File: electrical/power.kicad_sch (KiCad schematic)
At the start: 61 parts

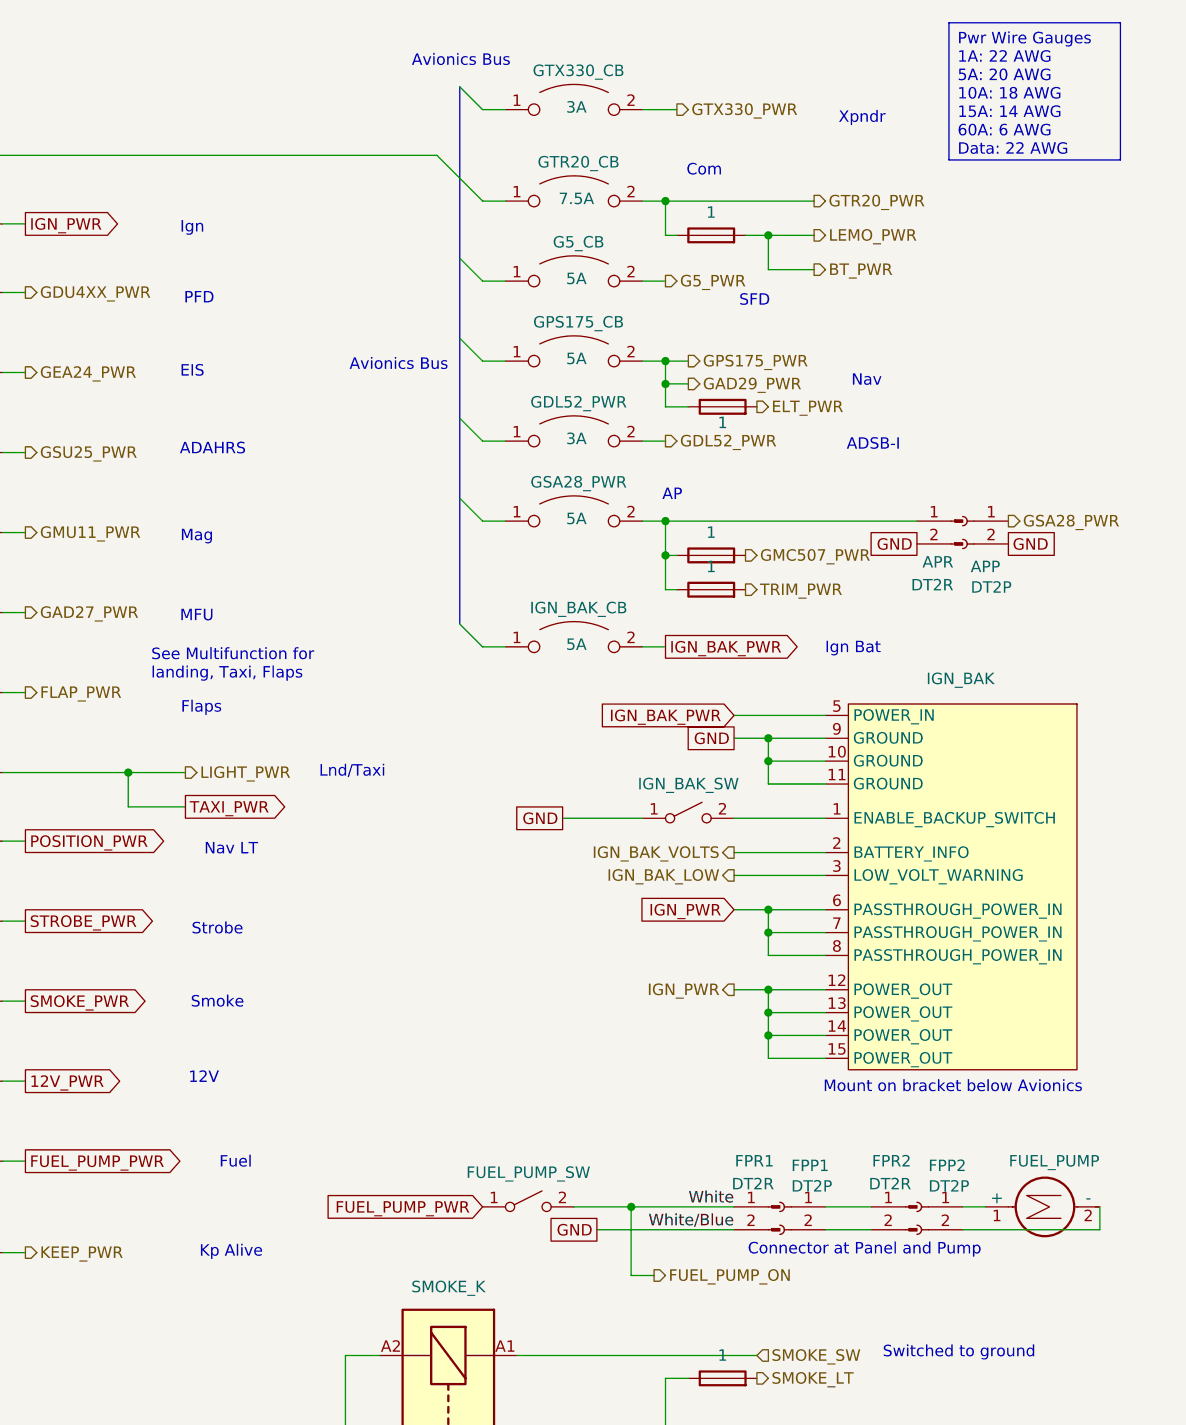
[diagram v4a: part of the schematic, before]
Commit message: Added AWG wires.
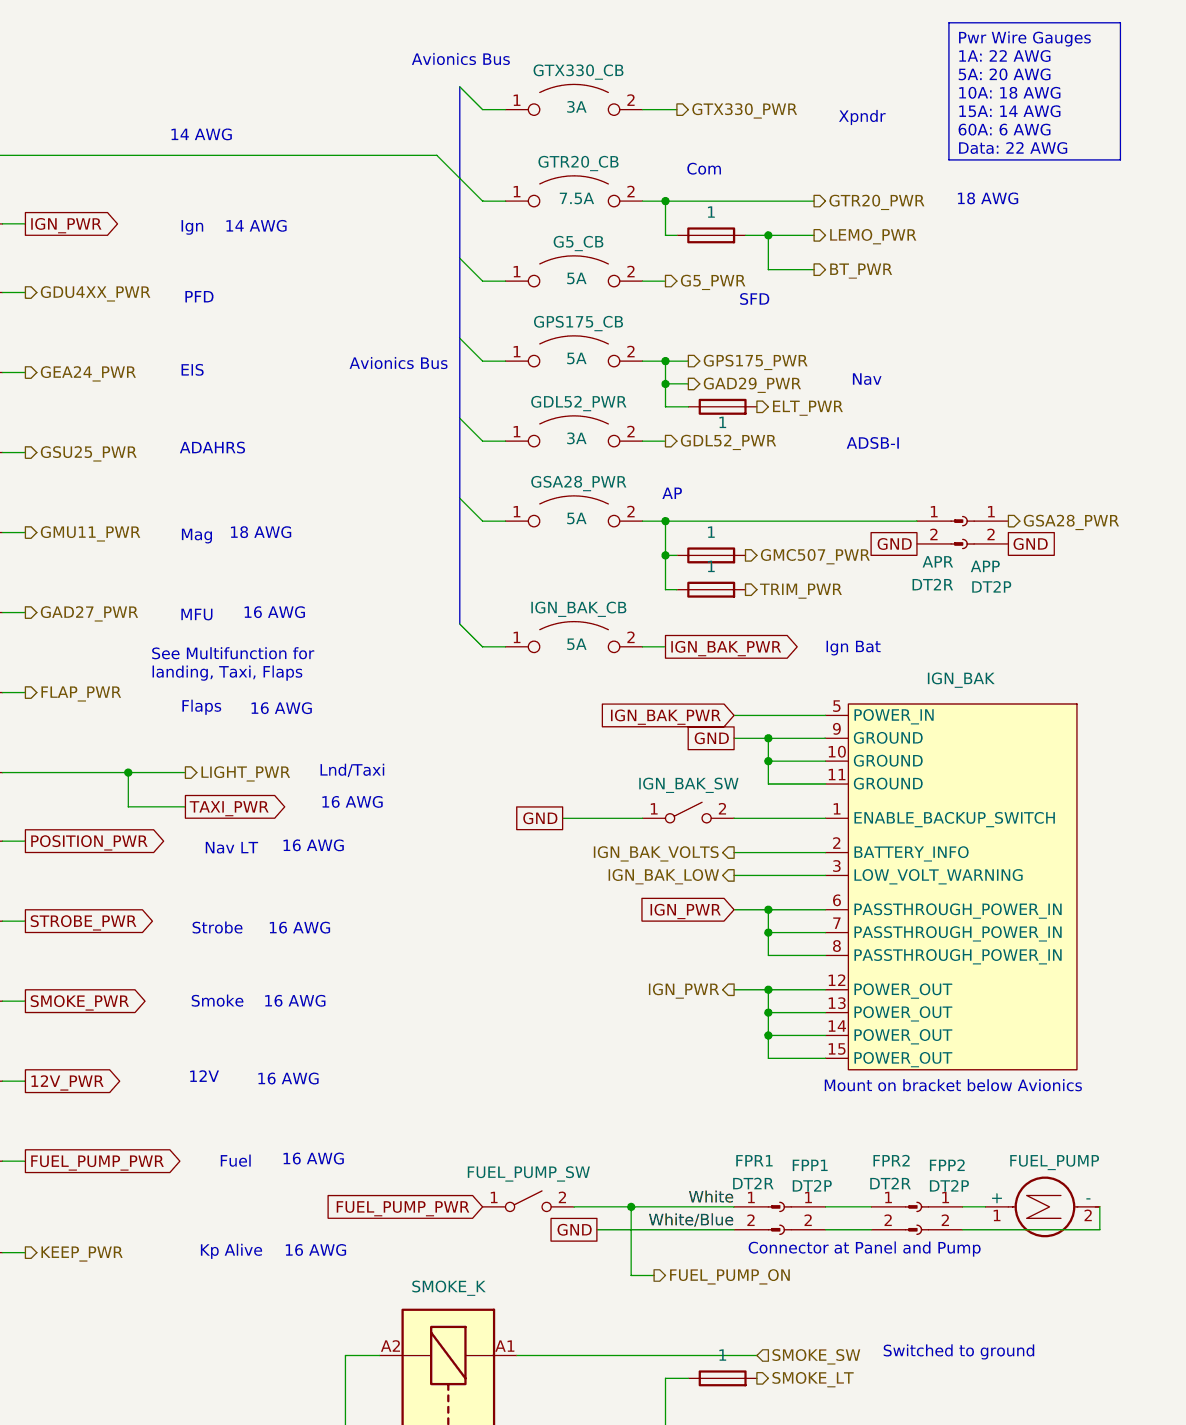
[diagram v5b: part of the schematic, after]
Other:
- note added: "14 AWG"
- note added: "16 AWG"
- note added: "18 AWG"
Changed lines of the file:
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@@
 		(title "Power Distribution")
 		(date "2025-12-24")
-		(rev "1.2")
+		(rev "1.2.1")
 		(company "N877RV")
 	)
@@
 		)
 	)
+	(text "16 AWG"
+		(exclude_from_sim no)
+		(at 109.982 123.444 0)
+		(effects
+			(font
+				(size 1.27 1.27)
+			)
+		)
+	)
 	(text "ADAHRS"
 		(exclude_from_sim no)
@@
 		)
 	)
+	(text "18 AWG"
+		(exclude_from_sim no)
+		(at 106.172 71.374 0)
+		(effects
+			(font
+				(size 1.27 1.27)
+			)
+		)
+	)
 	(text "Install small fuse box with 6 1A fuses\nInstall ground bar on both sides of firewall with 6AWG between"
 		(exclude_from_sim no)
@@
 		)
 	)
+	(text "16 AWG"
+		(exclude_from_sim no)
+		(at 107.696 80.264 0)
+		(effects
+			(font
+				(size 1.27 1.27)
+			)
+		)
+	)
 	(text "Nav"
 		(exclude_from_sim no)
@@
 		)
 	)
+	(text "16 AWG"
+		(exclude_from_sim no)
+		(at 109.22 132.08 0)
+		(effects
+			(font
+				(size 1.27 1.27)
+			)
+		)
+	)
 	(text "Ign"
 		(exclude_from_sim no)
@@
 		)
 	)
+	(text "14 AWG"
+		(exclude_from_sim no)
+		(at 99.568 27.178 0)
+		(effects
+			(font
+				(size 1.27 1.27)
+			)
+		)
+	)
+	(text "16 AWG"
+		(exclude_from_sim no)
+		(at 108.458 90.932 0)
+		(effects
+			(font
+				(size 1.27 1.27)
+			)
+		)
+	)
+	(text "16 AWG"
+		(exclude_from_sim no)
+		(at 112.014 140.97 0)
+		(effects
+			(font
+				(size 1.27 1.27)
+			)
+		)
+	)
+	(text "16 AWG"
+		(exclude_from_sim no)
+		(at 112.014 106.172 0)
+		(effects
+			(font
+				(size 1.27 1.27)
+			)
+		)
+	)
 	(text "Connector at Panel and Pump"
 		(exclude_from_sim no)
@@
 		)
 	)
+	(text "16 AWG"
+		(exclude_from_sim no)
+		(at 112.268 151.13 0)
+		(effects
+			(font
+				(size 1.27 1.27)
+			)
+		)
+	)
 	(text "Strobe"
 		(exclude_from_sim no)
@@
 		)
 	)
+	(text "16 AWG"
+		(exclude_from_sim no)
+		(at 116.332 101.346 0)
+		(effects
+			(font
+				(size 1.27 1.27)
+			)
+		)
+	)
 	(text "Switched to ground"
 		(exclude_from_sim no)
@@
 		)
 	)
+	(text "18 AWG"
+		(exclude_from_sim no)
+		(at 186.944 34.29 0)
+		(effects
+			(font
+				(size 1.27 1.27)
+			)
+		)
+	)
 	(text "Connector at Panel"
 		(exclude_from_sim no)
@@
 		)
 	)
+	(text "14 AWG"
+		(exclude_from_sim no)
+		(at 105.664 37.338 0)
+		(effects
+			(font
+				(size 1.27 1.27)
+			)
+		)
+	)
 	(text "Fuel"
 		(exclude_from_sim no)
@@
 		(effects
 			(font
+				(size 1.27 1.27)
+			)
+		)
+	)
+	(text "16 AWG"
+		(exclude_from_sim no)
+		(at 110.49 115.316 0)
+		(effects
+			(font

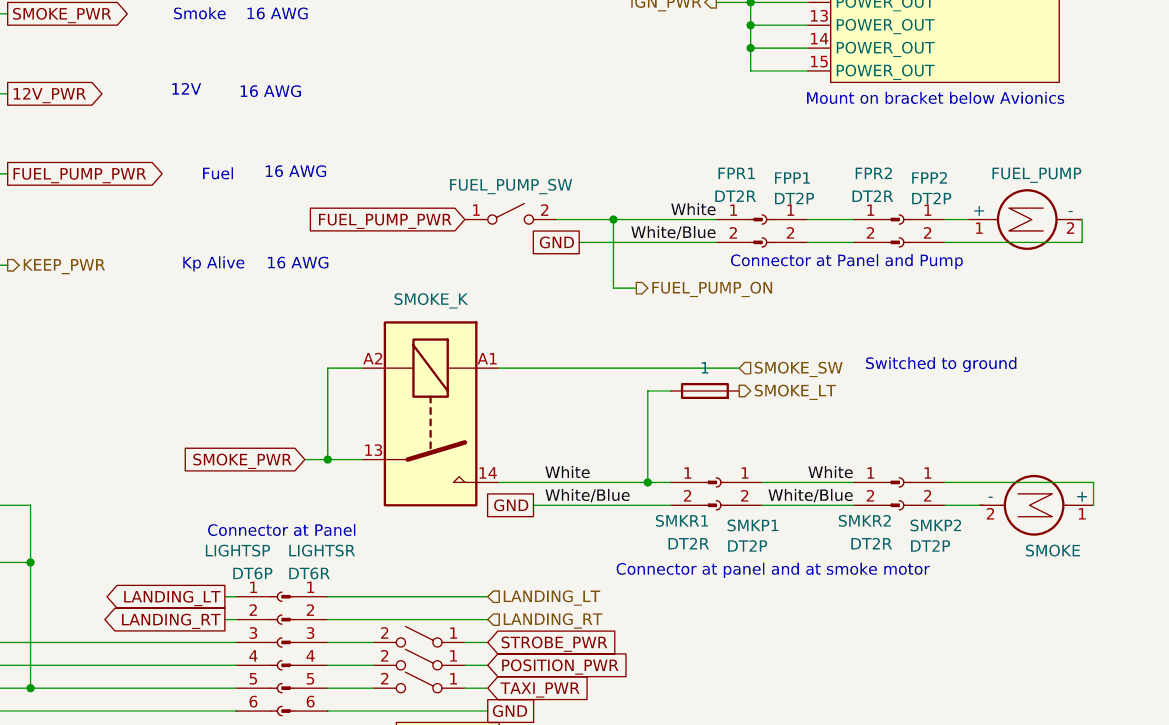
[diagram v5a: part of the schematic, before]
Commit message: Added extra connector for GDL 52, rewired stick to have flaps up/down instead of level/smoke. Put smoke on panel.
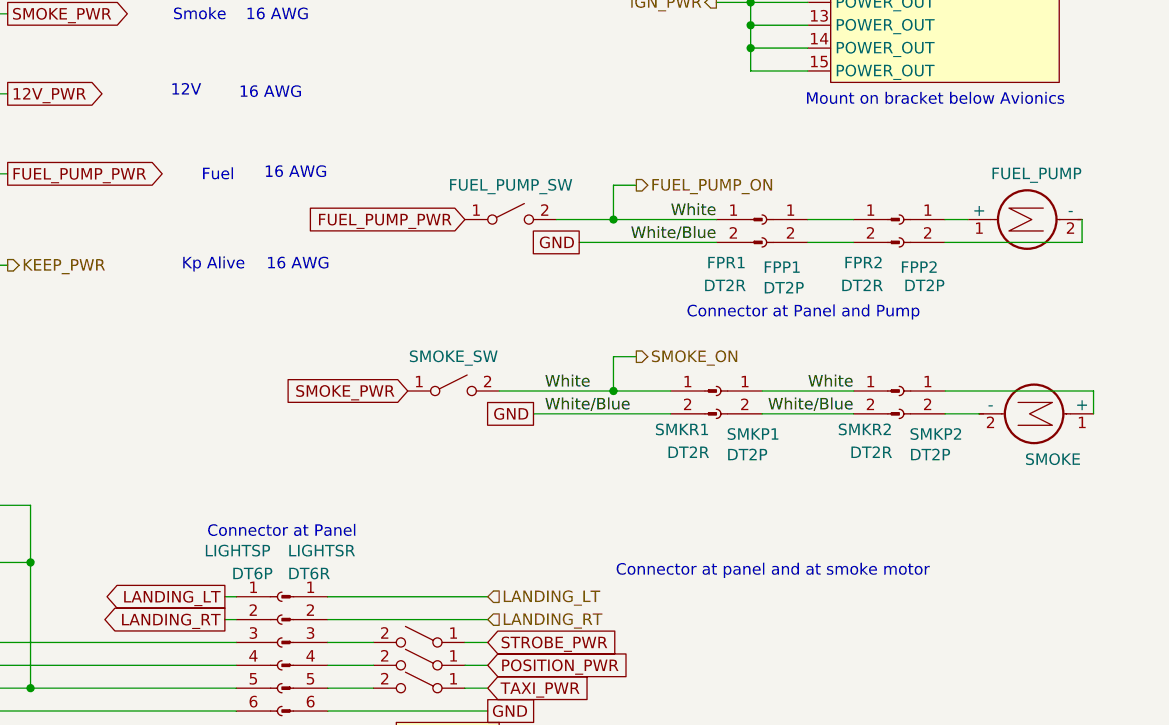
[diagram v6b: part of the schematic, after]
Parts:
- removed SMOKE_K: Relay_SPST-NO, symbol Relay:Relay_SPST-NO
- removed SMOKE_LT_FS: 1, symbol Device:Fuse
- added SMOKE_SW: ~, symbol Switch:SW_SPST
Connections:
- net FUEL_PUMP_ON: now also SMOKE_SW.2 (B)
- net SMOKE_PWR: now also SMOKE_SW.1 (A)
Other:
- note removed: "Switched to ground"
- moved on the sheet: SMKP1, SMKP2, SMKR1, SMKR2, SMOKE

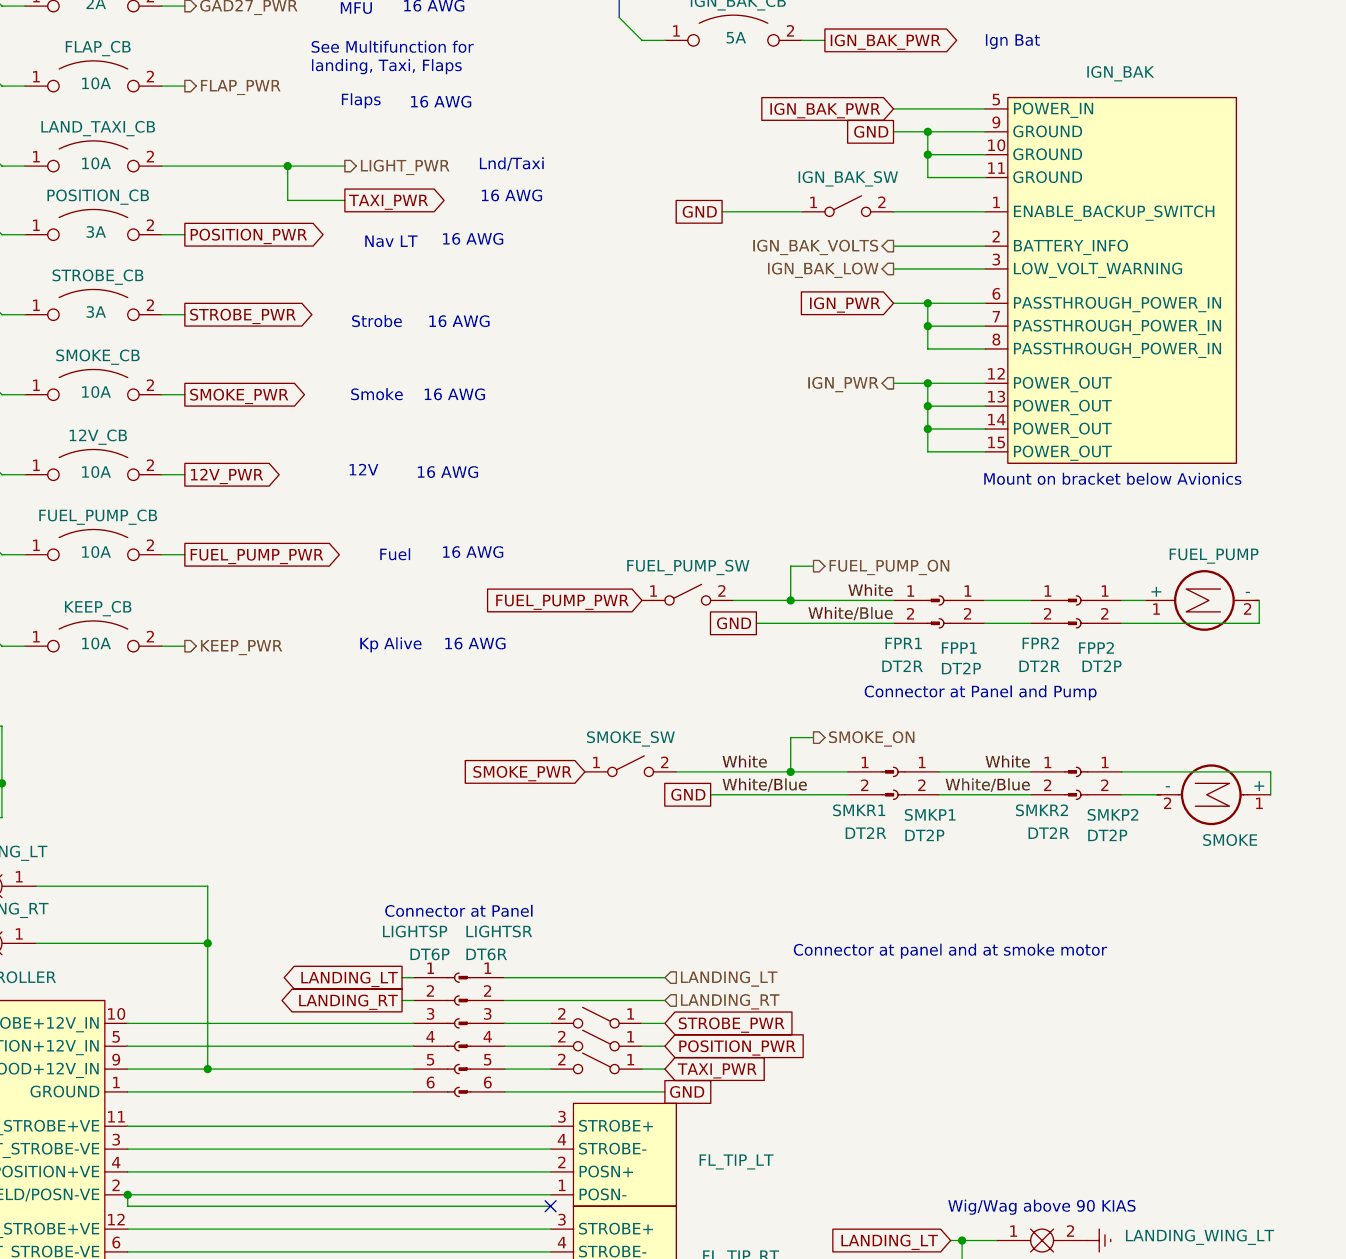
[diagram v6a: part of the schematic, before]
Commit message: Added beacon and added colors for flaps
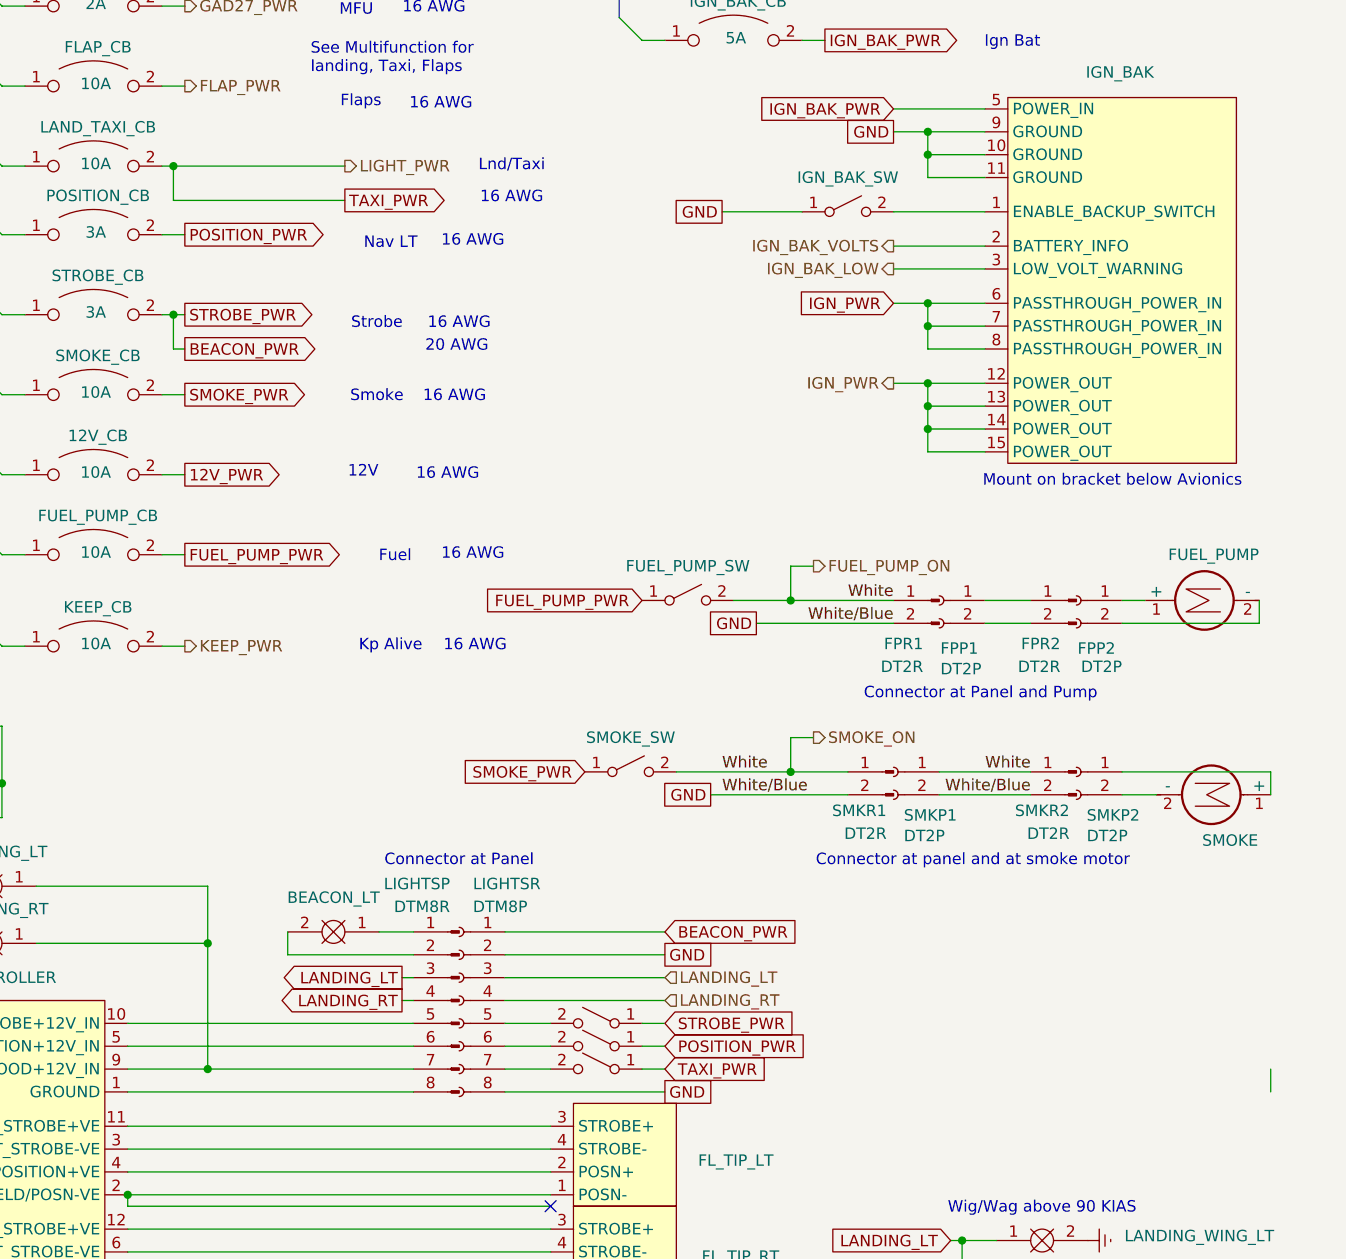
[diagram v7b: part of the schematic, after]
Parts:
- removed LIGHTSP: DT6P, symbol Connector:Conn_01x06_Socket
- removed LIGHTSR: DT6R, symbol Connector:Conn_01x06_Pin
- added BEACON_LT: Clear, symbol FlyerX:Bulb
- added LIGHTSP: DTM8R, symbol Connector:Conn_01x08_Pin
- added LIGHTSR: DTM8P, symbol Connector:Conn_01x08_Socket
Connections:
- net GND: now also LIGHTSR.2 (Pin_2), LIGHTSR.8 (Pin_8)
- net LANDING_LT: now also LIGHTSP.3 (Pin_3), LIGHTSR.3 (Pin_3)
- net LANDING_RT: now also LIGHTSP.4 (Pin_4), LIGHTSR.4 (Pin_4)
- net at STROBE_SW.2 (B): now also LIGHTSR.5 (Pin_5)
- net at FL_CONTROLLER.9 (FLOOD+12V_IN), TAXI_WING_LT.1, TAXI_WING_RT.1: now also LIGHTSP.7 (Pin_7)
- net at FL_CONTROLLER.10 (STROBE+12V_IN): now also LIGHTSP.5 (Pin_5)
- net at FL_CONTROLLER.5 (POSITION+12V_IN): now also LIGHTSP.6 (Pin_6)
- net at FL_CONTROLLER.1 (GROUND): now also LIGHTSP.8 (Pin_8)
- net at TAXI_SW.2 (B): now also LIGHTSR.7 (Pin_7)
- net at POSITION_SW.2 (B): now also LIGHTSR.6 (Pin_6)
- net STROBE_PWR renamed BEACON_PWR
- net BEACON_PWR: now also LIGHTSR.1 (Pin_1)
- new net: BEACON_LT.1, LIGHTSP.1 (Pin_1)
- new net: BEACON_LT.2, LIGHTSP.2 (Pin_2)
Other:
- note added: "20 AWG"
